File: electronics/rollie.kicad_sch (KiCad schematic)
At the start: 22 parts, among them J1 Jack-DC, J10 M-1, J11 Vcc (J2), J12 Vcc, J13 Relay In, J14 Motor 2, J15 Motor 1, J2 Vcc, J3 Probe, J4 Relay In, J5 Vcc (J12), J6 Serial, J7 Servo PWM, J8 Probe (J3), J9 M-2, K1 DIPxx-1Cxx-51x, SW1 SW_Push, U1 L298N

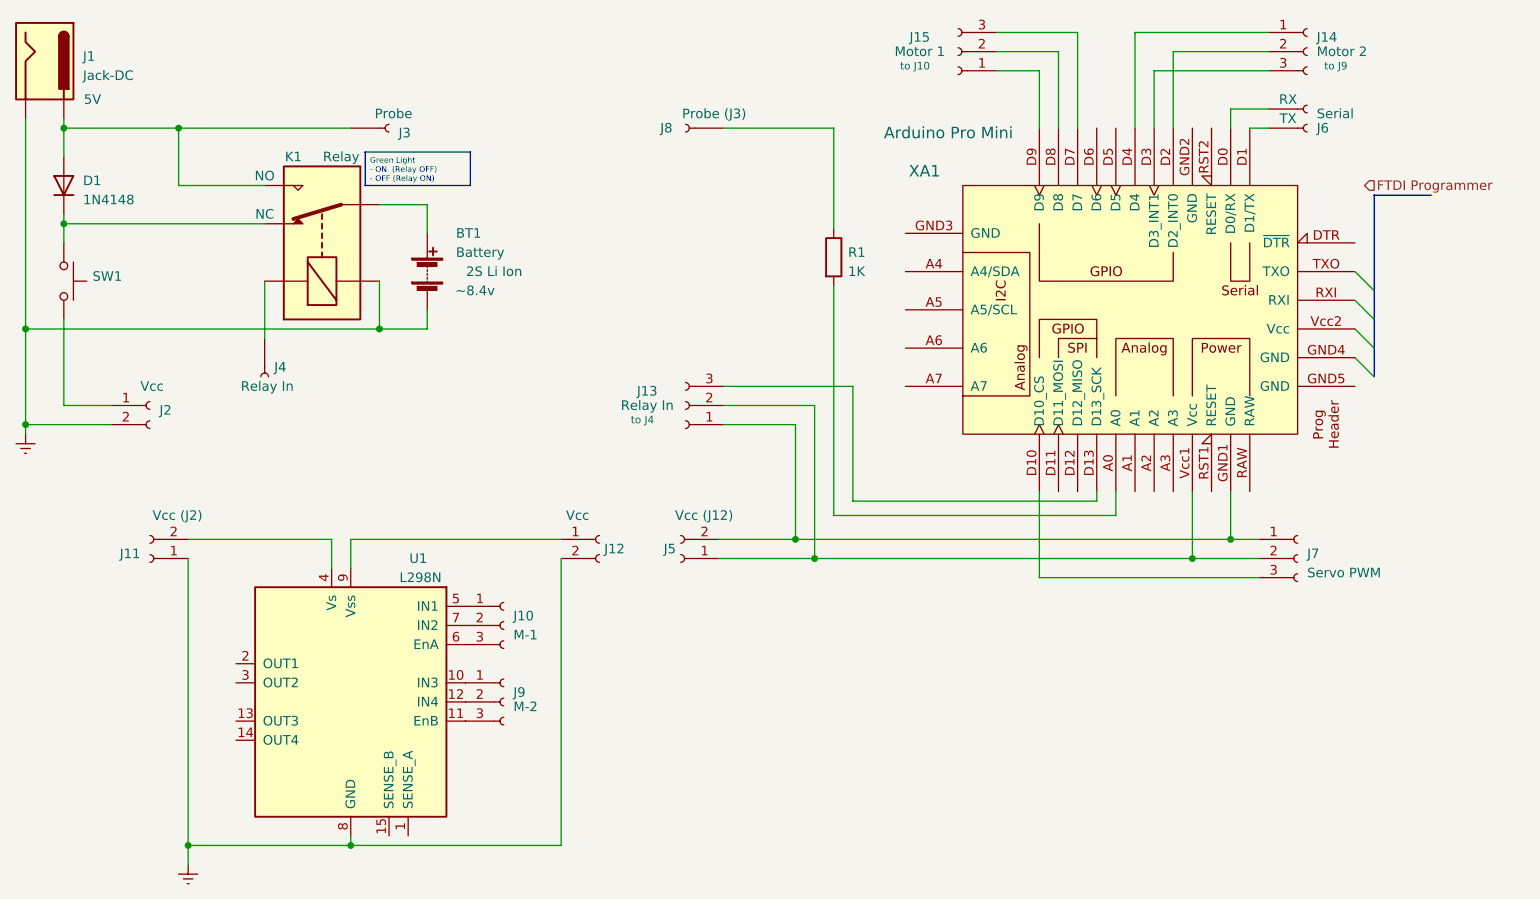
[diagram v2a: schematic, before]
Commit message: Adding GY-521 3 Axis IMU
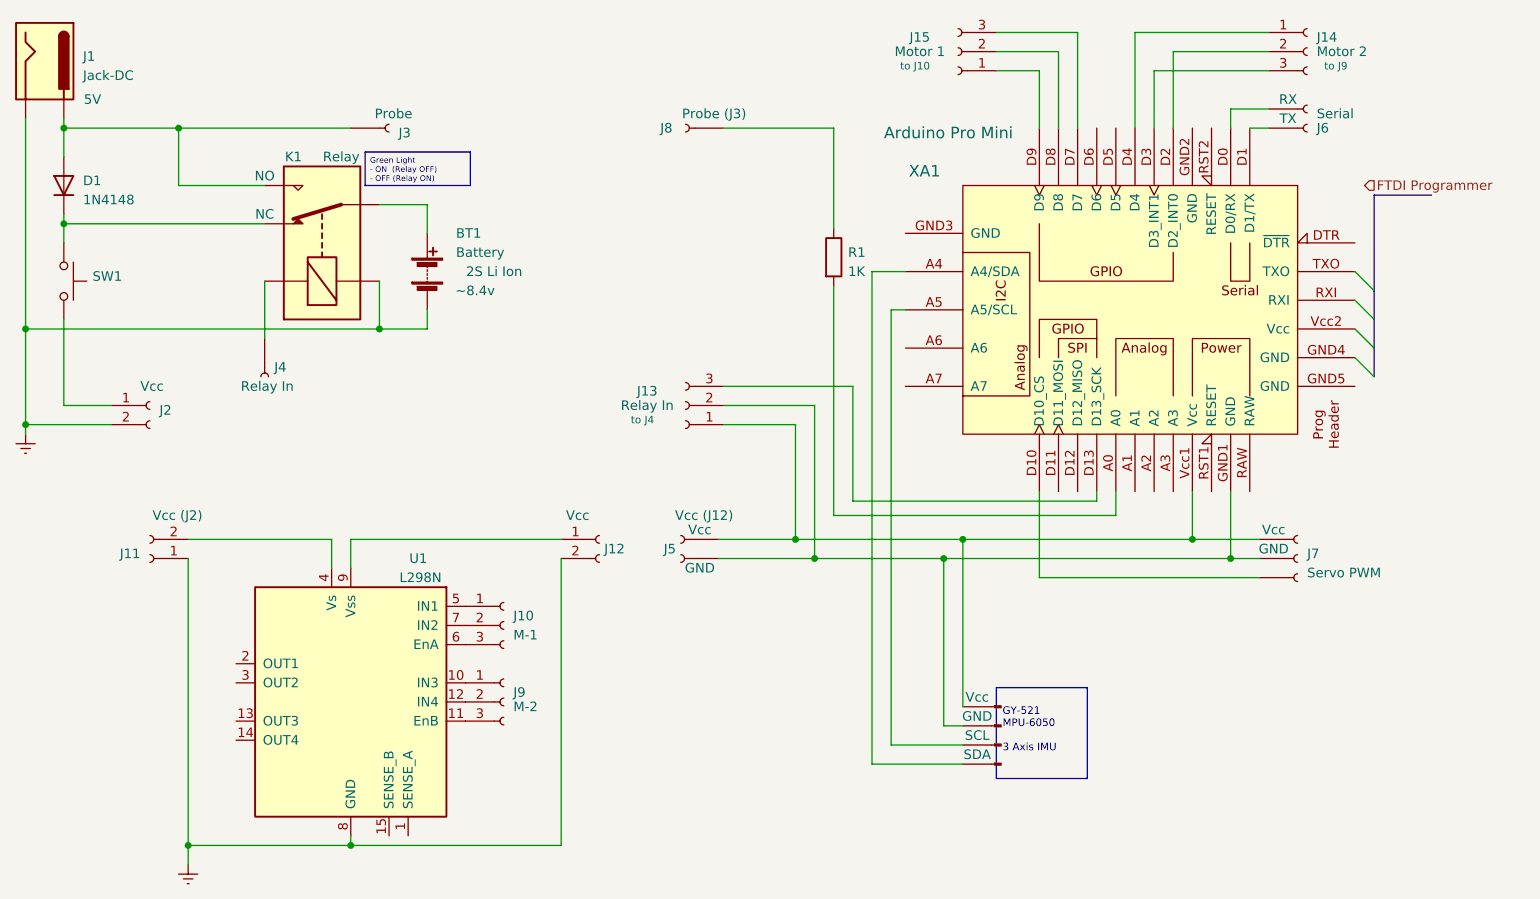
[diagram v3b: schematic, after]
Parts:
- added J16: Conn_01x04_Pin, symbol Connector:Conn_01x04_Pin
- J5, J7: GND (none) -> GND; Vcc (none) -> Vcc
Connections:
- net at J13.1 (Pin_1), J5.2 (Pin_2), J7.1 (Pin_1): now also XA1.Vcc1 (Vcc), J16.1 (Pin_1); no longer XA1.GND1 (GND)
- net at J13.2 (Pin_2), J5.1 (Pin_1), J7.2 (Pin_2): now also XA1.GND1 (GND), J16.2 (Pin_2); no longer XA1.Vcc1 (Vcc)
- net at XA1.A4 (A4/SDA): now also J16.4 (Pin_4)
- net at XA1.A5 (A5/SCL): now also J16.3 (Pin_3)
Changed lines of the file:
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@@
   (junction (at 25.4 68.58) (diameter 0) (color 0 0 0 0)
   )
+  (junction (at 147.32 86.36) (diameter 0) (color 0 0 0 0)
+  )
   (junction (at 68.58 124.46) (diameter 0) (color 0 0 0 0)
   )
+  (junction (at 149.86 83.82) (diameter 0) (color 0 0 0 0)
+  )
   (junction (at 45.72 29.21) (diameter 0) (color 0 0 0 0)
   )
+  (junction (at 185.42 86.36) (diameter 0) (color 0 0 0 0)
+  )
   (junction (at 30.48 41.91) (diameter 0) (color 0 0 0 0)
   )
-  (junction (at 180.34 86.36) (diameter 0) (color 0 0 0 0)
-  )
   (junction (at 25.4 55.88) (diameter 0) (color 0 0 0 0)
   )
+  (junction (at 180.34 83.82) (diameter 0) (color 0 0 0 0)
+  )
   (junction (at 127.635 83.82) (diameter 0) (color 0 0 0 0)
   )
-  (junction (at 185.42 83.82) (diameter 0) (color 0 0 0 0)
-  )
   (junction (at 130.175 86.36) (diameter 0) (color 0 0 0 0)
   )
@@
     (stroke (width 0) (type default))
   )
-  (wire (pts (xy 180.34 77.47) (xy 180.34 86.36))
+  (wire (pts (xy 147.32 86.36) (xy 147.32 108.585))
     (stroke (width 0) (type default))
   )
@@
     (stroke (width 0) (type default))
   )
+  (wire (pts (xy 140.335 111.125) (xy 140.335 53.34))
+    (stroke (width 0) (type default))
+  )
   (wire (pts (xy 165.1 16.51) (xy 154.305 16.51))
     (stroke (width 0) (type default))
@@
     (stroke (width 0) (type default))
   )
+  (wire (pts (xy 185.42 77.47) (xy 185.42 86.36))
+    (stroke (width 0) (type default))
+  )
   (wire (pts (xy 78.74 43.18) (xy 78.74 39.37))
     (stroke (width 0) (type default))
   )
-  (wire (pts (xy 185.42 83.82) (xy 189.23 83.82))
+  (wire (pts (xy 180.34 83.82) (xy 189.23 83.82))
     (stroke (width 0) (type default))
   )
@@
     (stroke (width 0) (type default))
   )
+  (wire (pts (xy 147.32 86.36) (xy 185.42 86.36))
+    (stroke (width 0) (type default))
+  )
   (wire (pts (xy 118.11 68.58) (xy 127.635 68.58))
     (stroke (width 0) (type default))
   )
+  (wire (pts (xy 185.42 86.36) (xy 189.23 86.36))
+    (stroke (width 0) (type default))
+  )
   (wire (pts (xy 25.4 55.88) (xy 72.39 55.88))
     (stroke (width 0) (type default))
   )
+  (wire (pts (xy 149.86 83.82) (xy 149.86 106.045))
+    (stroke (width 0) (type default))
+  )
   (wire (pts (xy 25.4 55.88) (xy 25.4 68.58))
     (stroke (width 0) (type default))
@@
     (stroke (width 0) (type default))
   )
+  (wire (pts (xy 142.24 48.26) (xy 137.795 48.26))
+    (stroke (width 0) (type default))
+  )
+  (wire (pts (xy 130.175 86.36) (xy 147.32 86.36))
+    (stroke (width 0) (type default))
+  )
   (wire (pts (xy 185.42 29.21) (xy 185.42 26.67))
     (stroke (width 0) (type default))
@@
     (stroke (width 0) (type default))
   )
-  (wire (pts (xy 185.42 77.47) (xy 185.42 83.82))
-    (stroke (width 0) (type default))
-  )
   (wire (pts (xy 185.42 26.67) (xy 190.5 26.67))
     (stroke (width 0) (type default))
@@
     (stroke (width 0) (type default))
   )
+  (wire (pts (xy 180.34 77.47) (xy 180.34 83.82))
+    (stroke (width 0) (type default))
+  )
   (wire (pts (xy 30.48 40.64) (xy 30.48 41.91))
     (stroke (width 0) (type default))
@@
     (stroke (width 0) (type default))
   )
-  (wire (pts (xy 180.34 86.36) (xy 189.23 86.36))
-    (stroke (width 0) (type default))
-  )
   (wire (pts (xy 25.4 27.94) (xy 25.4 55.88))
     (stroke (width 0) (type default))
@@
     (stroke (width 0) (type default))
   )
+  (wire (pts (xy 149.86 108.585) (xy 147.32 108.585))
+    (stroke (width 0) (type default))
+  )
   (wire (pts (xy 45.72 29.21) (xy 30.48 29.21))
     (stroke (width 0) (type default))
   )
+  (wire (pts (xy 140.335 53.34) (xy 142.24 53.34))
+    (stroke (width 0) (type default))
+  )
   (wire (pts (xy 170.18 77.47) (xy 170.18 80.645))
     (stroke (width 0) (type default))
@@
     (stroke (width 0) (type default))
   )
+  (wire (pts (xy 137.795 113.665) (xy 149.86 113.665))
+    (stroke (width 0) (type default))
+  )
   (wire (pts (xy 132.715 29.21) (xy 118.11 29.21))
     (stroke (width 0) (type default))
@@
     (stroke (width 0) (type default))
   )
+  (wire (pts (xy 127.635 83.82) (xy 149.86 83.82))
+    (stroke (width 0) (type default))
+  )
   (bus (pts (xy 204.47 62.23) (xy 204.47 58.42))
     (stroke (width 0) (type default))
@@
     (stroke (width 0) (type default))
   )
-  (wire (pts (xy 127.635 83.82) (xy 185.42 83.82))
-    (stroke (width 0) (type default))
-  )
   (wire (pts (xy 72.39 49.53) (xy 72.39 55.88))
     (stroke (width 0) (type default))
@@
     (stroke (width 0) (type default))
   )
+  (wire (pts (xy 149.86 83.82) (xy 180.34 83.82))
+    (stroke (width 0) (type default))
+  )
   (bus (pts (xy 204.47 38.1) (xy 212.09 38.1))
     (stroke (width 0) (type default))
@@
     (stroke (width 0) (type default))
   )
+  (wire (pts (xy 137.795 48.26) (xy 137.795 113.665))
+    (stroke (width 0) (type default))
+  )
+  (wire (pts (xy 149.86 111.125) (xy 140.335 111.125))
+    (stroke (width 0) (type default))
+  )
   (wire (pts (xy 160.02 21.59) (xy 154.305 21.59))
     (stroke (width 0) (type default))
@@
     (stroke (width 0) (type default))
   )
-  (wire (pts (xy 130.175 86.36) (xy 180.34 86.36))
-    (stroke (width 0) (type default))
-  )
   (wire (pts (xy 57.15 36.83) (xy 45.72 36.83))
     (stroke (width 0) (type default))
@@
   (wire (pts (xy 170.18 80.645) (xy 132.715 80.645))
     (stroke (width 0) (type default))
+  )
+  (text_box "\n  GY-521\n  MPU-6050\n\n  3 Axis IMU"
+    (at 154.305 103.505 0) (size 12.065 12.065)
+    (stroke (width 0.1) (type default) (color 132 0 0 1))
+    (fill (type color) (color 255 251 183 1))
+    (effects (font (size 1 1) (color 132 0 0 1)) (justify left top))
   )
   (text_box "Green Light\n- ON  (Relay OFF)\n- OFF (Relay ON)"
@@
         (path "/21ef0648-144d-4869-9598-e74abff26616"
           (reference "J3") (unit 1)
+        )
+      )
+    )
+  )
+  (symbol (lib_id "Connector:Conn_01x04_Pin") (at 154.94 108.585 0) (mirror y) (unit 1)
+    (in_bom yes) (on_board yes) (dnp no)
+    (property "Reference" "J16" (at 150.495 100.965 0)
+      (effects (font (size 1.27 1.27)) hide)
+    )
+    (property "Value" "Conn_01x04_Pin" (at 161.29 101.6 0)
+      (effects (font (size 1.27 1.27)) hide)
+    )
+    (property "Footprint" "" (at 154.94 108.585 0)
+      (effects (font (size 1.27 1.27)) hide)
+    )
+    (property "Datasheet" "~" (at 154.94 108.585 0)
+      (effects (font (size 1.27 1.27)) hide)
+    )
+    (property "Vcc" "Vcc" (at 151.765 104.775 0)
+      (effects (font (size 1.27 1.27)))
+    )
+    (property "Gnd" "GND" (at 151.765 107.315 0)
+      (effects (font (size 1.27 1.27)))
+    )
+    (property "SCL" "SCL" (at 151.765 109.855 0)
+      (effects (font (size 1.27 1.27)))
+    )
+    (property "SDA" "SDA" (at 151.765 112.395 0)
+      (effects (font (size 1.27 1.27)))
+    )
+    (pin "1")
+    (pin "2")
+    (pin "3")
+    (pin "4")
+    (instances
+      (project "rollie"
+        (path "/21ef0648-144d-4869-9598-e74abff26616"
+          (reference "J16") (unit 1)
         )
       )
@@
     )
   )
-  (symbol (lib_id "Connector:Conn_01x02_Socket") (at 112.395 86.36 180) (unit 1)
+  (symbol (lib_name "Conn_01x02_Socket_2") (lib_id "Connector:Conn_01x02_Socket") (at 112.395 86.36 180) (unit 1)
     (in_bom yes) (on_board yes) (dnp no)
     (property "Reference" "J5" (at 111.76 85.09 0)
@@
     (property "Datasheet" "~" (at 112.395 86.36 0)
       (effects (font (size 1.27 1.27)) hide)
+    )
+    (property "Vcc" "Vcc" (at 114.935 82.55 0)
+      (effects (font (size 1.27 1.27)))
+    )
+    (property "GND" "GND" (at 114.935 87.63 0)
+      (effects (font (size 1.27 1.27)))
     )
     (pin "1")
@@
     )
   )
-  (symbol (lib_id "Connector:Conn_01x03_Socket") (at 194.31 86.36 0) (unit 1)
-    (in_bom yes) (on_board yes) (dnp no) (fields_autoplaced)
+  (symbol (lib_name "Conn_01x03_Socket_1") (lib_id "Connector:Conn_01x03_Socket") (at 194.31 86.36 0) (unit 1)
+    (in_bom yes) (on_board yes) (dnp no)
     (property "Reference" "J7" (at 195.58 85.725 0)
       (effects (font (size 1.27 1.27)) (justify left))
@@
       (effects (font (size 1.27 1.27)) hide)
     )
-    (pin "1")
+    (property "Vcc" "Vcc" (at 191.135 82.55 0)
+      (effects (font (size 1.27 1.27)))
+    )
+    (property "GND" "GND" (at 191.135 85.09 0)
+      (effects (font (size 1.27 1.27)))
+    )
+    (pin "1")
